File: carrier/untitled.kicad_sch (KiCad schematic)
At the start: 9 parts

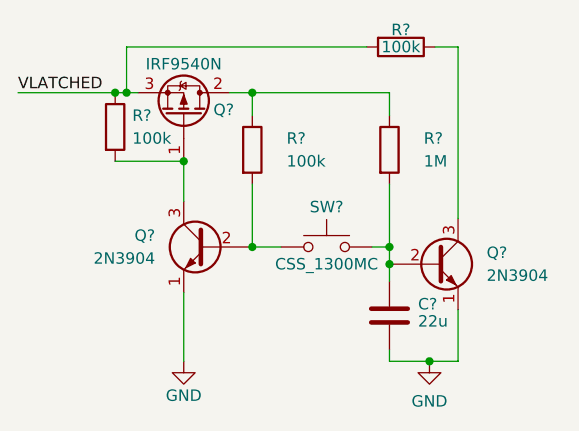
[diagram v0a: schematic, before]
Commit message: fixed switching and added fuel gague
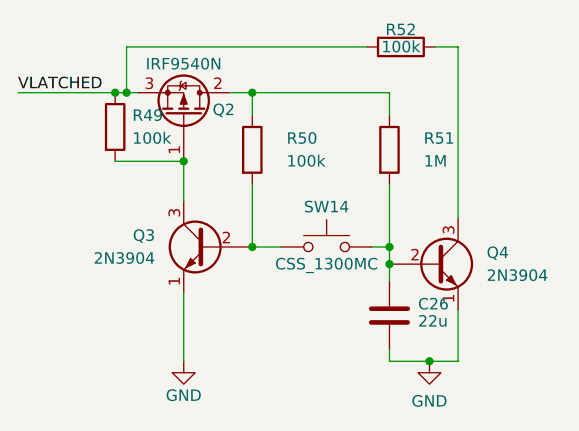
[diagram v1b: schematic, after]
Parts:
- gave numbers to parts that had none: 9
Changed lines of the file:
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@@
 (kicad_sch (version 20210621) (generator eeschema)
   (paper "A4")
-  (junction (at 151.13 109.855) (diameter 0) (color 0 0 0 0))
-  (junction (at 137.16 92.71) (diameter 0) (color 0 0 0 0))
-  (junction (at 166.37 109.855) (diameter 0) (color 0 0 0 0))
+  (junction (at 151.13 92.71) (diameter 0) (color 0 0 0 0))
+  (junction (at 170.815 122.555) (diameter 0) (color 0 0 0 0))
   (junction (at 166.37 111.76) (diameter 0) (color 0 0 0 0))
   (junction (at 143.51 100.33) (diameter 0) (color 0 0 0 0))
-  (junction (at 170.815 122.555) (diameter 0) (color 0 0 0 0))
-  (junction (at 151.13 92.71) (diameter 0) (color 0 0 0 0))
   (junction (at 135.89 92.71) (diameter 0) (color 0 0 0 0))
+  (junction (at 137.16 92.71) (diameter 0) (color 0 0 0 0))
+  (junction (at 151.13 109.855) (diameter 0) (color 0 0 0 0))
+  (junction (at 166.37 109.855) (diameter 0) (color 0 0 0 0))
   (wire (pts (xy 166.37 121.285) (xy 166.37 122.555))
     (stroke (width 0) (type default) (color 0 0 0 0))
@@
   (symbol (lib_id "Device:R") (at 135.89 96.52 0) (unit 1)
     (in_bom yes) (on_board yes)
-    (property "Reference" "R?" (id 0) (at 137.795 95.25 0)
+    (property "Reference" "R49" (id 0) (at 137.795 95.25 0)
       (effects (font (size 1.27 1.27)) (justify left))
     )
@@
   (symbol (lib_id "Device:R") (at 167.64 87.63 270) (unit 1)
     (in_bom yes) (on_board yes)
-    (property "Reference" "R?" (id 0) (at 167.64 85.725 90))
+    (property "Reference" "R52" (id 0) (at 167.64 85.725 90))
     (property "Value" "100k" (id 1) (at 167.64 87.63 90))
     (property "Footprint" "" (id 2) (at 167.64 85.852 90)
@@
   (symbol (lib_id "Device:R") (at 166.37 99.06 0) (unit 1)
     (in_bom yes) (on_board yes) (fields_autoplaced)
-    (property "Reference" "R?" (id 0) (at 170.18 97.79 0)
+    (property "Reference" "R51" (id 0) (at 170.18 97.79 0)
       (effects (font (size 1.27 1.27)) (justify left))
     )
@@
   (symbol (lib_id "power:GND") (at 170.815 122.555 0) (unit 1)
     (in_bom yes) (on_board yes)
-    (property "Reference" "#PWR?" (id 0) (at 170.815 128.905 0)
+    (property "Reference" "#PWR047" (id 0) (at 170.815 128.905 0)
       (effects (font (size 1.27 1.27)) hide)
     )
@@
   (symbol (lib_id "power:GND") (at 143.51 122.555 0) (unit 1)
     (in_bom yes) (on_board yes)
-    (property "Reference" "#PWR?" (id 0) (at 143.51 128.905 0)
+    (property "Reference" "#PWR046" (id 0) (at 143.51 128.905 0)
       (effects (font (size 1.27 1.27)) hide)
     )
@@
   (symbol (lib_id "Transistor_FET:IRF9540N") (at 143.51 95.25 270) (mirror x) (unit 1)
     (in_bom yes) (on_board yes)
-    (property "Reference" "Q?" (id 0) (at 147.955 94.615 90))
+    (property "Reference" "Q2" (id 0) (at 147.955 94.615 90))
     (property "Value" "IRF9540N" (id 1) (at 143.51 89.535 90))
     (property "Footprint" "Package_TO_SOT_THT:TO-220-3_Vertical" (id 2) (at 141.605 90.17 0)
@@
   (symbol (lib_id "Transistor_BJT:2N3904") (at 171.45 111.76 0) (unit 1)
     (in_bom yes) (on_board yes)
-    (property "Reference" "Q?" (id 0) (at 177.165 110.49 0)
+    (property "Reference" "Q4" (id 0) (at 177.165 110.49 0)
       (effects (font (size 1.27 1.27)) (justify left))
     )
@@
   (symbol (lib_id "Switch:SW_Push") (at 159.385 109.855 0) (unit 1)
     (in_bom yes) (on_board yes)
-    (property "Reference" "SW?" (id 0) (at 159.385 105.41 0))
+    (property "Reference" "SW14" (id 0) (at 159.385 105.41 0))
     (property "Value" "CSS_1300MC" (id 1) (at 159.385 111.76 0))
     (property "Footprint" "" (id 2) (at 159.385 104.775 0)
@@
   (symbol (lib_id "Transistor_BJT:2N3904") (at 146.05 109.855 0) (mirror y) (unit 1)
     (in_bom yes) (on_board yes)
-    (property "Reference" "Q?" (id 0) (at 140.335 108.585 0)
+    (property "Reference" "Q3" (id 0) (at 140.335 108.585 0)
       (effects (font (size 1.27 1.27)) (justify left))
     )
@@
   (symbol (lib_id "Device:C") (at 166.37 117.475 0) (unit 1)
     (in_bom yes) (on_board yes)
-    (property "Reference" "C?" (id 0) (at 169.545 116.205 0)
+    (property "Reference" "C26" (id 0) (at 169.545 116.205 0)
       (effects (font (size 1.27 1.27)) (justify left))
     )
@@
   (symbol (lib_id "Device:R") (at 151.13 99.06 0) (unit 1)
     (in_bom yes) (on_board yes) (fields_autoplaced)
-    (property "Reference" "R?" (id 0) (at 154.94 97.79 0)
-      (effects (font (size 1.27 1.27)) (justify left))
-    )
+    (property "Reference" "R50" (id 0) (at 154.94 97.79 0)
+      (effects (font (size 1.27 1.27)) (justify left))
+    )
